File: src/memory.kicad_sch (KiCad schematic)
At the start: 8 parts, among them Q1 NPN, Q2 NPN, SW1 SW_Push, SW2 SW_Push

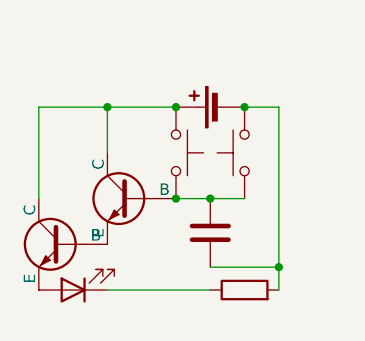
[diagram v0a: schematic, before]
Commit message: Update entire PCB
README not updated
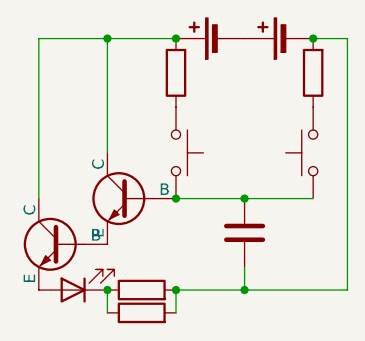
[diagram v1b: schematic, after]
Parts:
- added BT2: Battery_Cell, Battery:BatteryHolder_Keystone_3034_1x20mm, symbol Device:Battery_Cell
- added R2, R3, R4: R, Resistor_THT:R_Axial_DIN0207_L6.3mm_D2.5mm_P7.62mm_Horizontal, symbol Device:R
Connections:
- net at BT1.1 (+), Q1.1 (C), Q2.1 (C): now also R3.2; no longer SW1.1
- net at D1.1 (K), R1.1: now also R2.1
- net at C1.2, R1.2: now also BT2.2 (-), R2.2, R4.2; no longer BT1.2 (-), SW2.2
- new net: R4.1, SW2.2
- new net: BT1.2 (-), BT2.1 (+)
- new net: R3.1, SW1.1
